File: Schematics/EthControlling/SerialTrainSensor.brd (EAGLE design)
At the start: 13 x 23 mm, 17 parts, among them IC2 LMV358

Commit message: identify schematics by the order number on schematics and submitted gerber files
Signed-off-by: sosoru <siva6991@yahoo.co.jp>
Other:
- board text added: "D53371"
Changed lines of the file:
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@@
 <text x="11.5824" y="7.7216" size="0.6096" layer="21" font="vector" rot="R270">TrSensor Rev.B</text>
 <text x="10.3632" y="2.8448" size="0.6096" layer="21" font="vector" rot="R270">T.U.S.</text>
+<text x="8.7376" y="11.5824" size="1.016" layer="26" rot="MR0">D53371</text>
 </plain>
 <attributes>

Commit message: debuging device transfer
Signed-off-by: sosoru <siva6991@yahoo.co.jp>
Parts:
- R1, R5: value (none) -> 1k
- R2, R6: value (none) -> 100k
- R3, R4: value (none) -> 33k
- R7: value (none) -> 10k
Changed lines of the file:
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@@
 <attribute name="VALUE" x="3.6282" y="0.256" size="0.6096" layer="21" font="vector" rot="R90"/>
 </element>
-<element name="R3" library="rcl" package="R0603" value="" x="4.3688" y="16.8656" smashed="yes" rot="R180">
+<element name="R3" library="rcl" package="R0603" value="33k" x="4.3688" y="16.8656" smashed="yes" rot="R180">
 <attribute name="NAME" x="2.9718" y="17.2466" size="0.6096" layer="25" font="vector" rot="R180"/>
 <attribute name="VALUE" x="5.0038" y="18.7706" size="1.27" layer="27" rot="R180"/>
 </element>
-<element name="R1" library="rcl" package="R0603" value="" x="4.3688" y="18.1864" smashed="yes" rot="R180">
+<element name="R1" library="rcl" package="R0603" value="1k" x="4.3688" y="18.1864" smashed="yes" rot="R180">
 <attribute name="NAME" x="2.9718" y="18.5674" size="0.6096" layer="25" font="vector" rot="R180"/>
 <attribute name="VALUE" x="5.0038" y="20.0914" size="1.27" layer="27" rot="R180"/>
 </element>
-<element name="R2" library="rcl" package="R0603" value="" x="2.032" y="20.7264" smashed="yes" rot="R90">
+<element name="R2" library="rcl" package="R0603" value="100k" x="2.032" y="20.7264" smashed="yes" rot="R90">
 <attribute name="NAME" x="1.397" y="20.0914" size="0.6096" layer="25" font="vector" rot="R90"/>
 <attribute name="VALUE" x="3.937" y="20.0914" size="1.27" layer="27" rot="R90"/>
 </element>
-<element name="R6" library="rcl" package="R0603" value="" x="6.9088" y="2.032" smashed="yes" rot="R270">
+<element name="R6" library="rcl" package="R0603" value="100k" x="6.9088" y="2.032" smashed="yes" rot="R270">
 <attribute name="NAME" x="7.5438" y="2.667" size="0.6096" layer="25" font="vector" rot="R270"/>
 <attribute name="VALUE" x="5.0038" y="2.667" size="1.27" layer="27" rot="R270"/>
 </element>
-<element name="R4" library="rcl" package="R0603" value="" x="4.064" y="6.9088" smashed="yes" rot="R180">
+<element name="R4" library="rcl" package="R0603" value="33k" x="4.064" y="6.9088" smashed="yes" rot="R180">
 <attribute name="NAME" x="2.667" y="7.493" size="0.6096" layer="25" font="vector" rot="R180"/>
 <attribute name="VALUE" x="4.699" y="8.8138" size="1.27" layer="27" rot="R180"/>
 </element>
-<element name="R5" library="rcl" package="R0603" value="" x="4.064" y="5.4864" smashed="yes">
+<element name="R5" library="rcl" package="R0603" value="1k" x="4.064" y="5.4864" smashed="yes">
 <attribute name="NAME" x="1.6002" y="5.5118" size="0.6096" layer="25" font="vector"/>
 <attribute name="VALUE" x="3.429" y="3.5814" size="1.27" layer="27"/>
@@
 <element name="SMD1" library="myparts" package="SERIAL_5_HALF" value="SERIAL_SENSORHALF" x="11.7856" y="11.7856" rot="R90"/>
 <element name="SMD2" library="myparts" package="SERIAL_5_HALF" value="SERIAL_SENSORHALF" x="1.2192" y="11.7856" rot="R90"/>
-<element name="R7" library="rcl" package="R0603" value="" x="8.636" y="12.5984" smashed="yes" rot="R180">
+<element name="R7" library="rcl" package="R0603" value="10k" x="8.636" y="12.5984" smashed="yes" rot="R180">
 <attribute name="NAME" x="10.0838" y="13.9954" size="0.6096" layer="25" font="vector" rot="R180"/>
 <attribute name="VALUE" x="9.271" y="14.5034" size="1.27" layer="27" rot="R180"/>

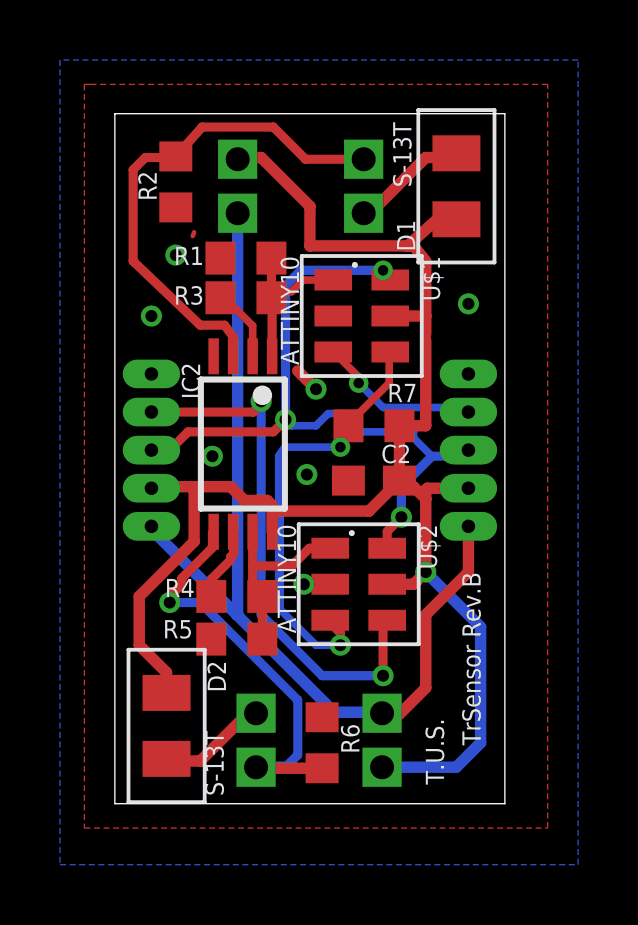
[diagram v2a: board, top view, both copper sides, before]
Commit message: fixed train sensor board
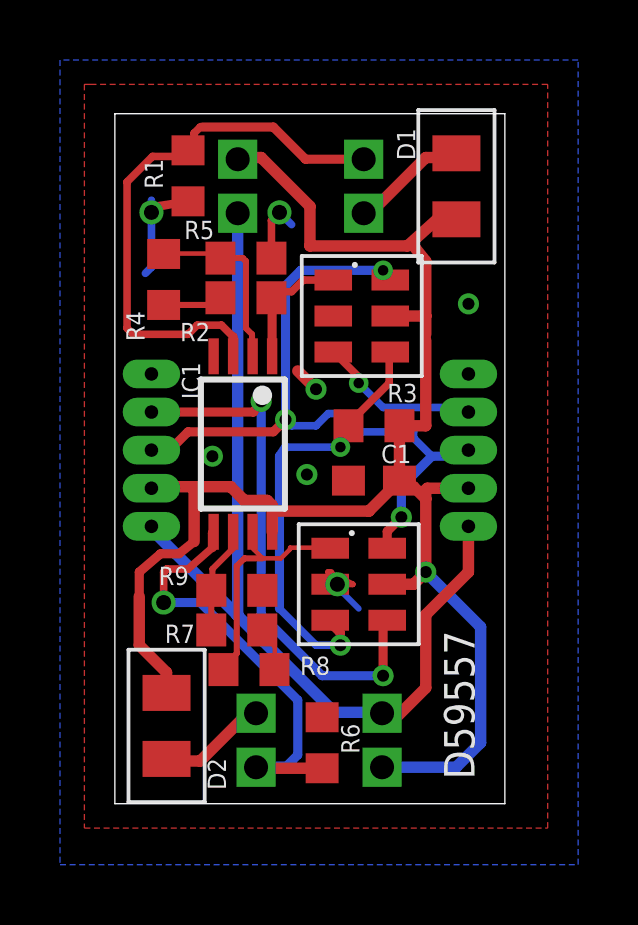
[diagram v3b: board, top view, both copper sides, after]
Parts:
- removed U$101: TPR-105F, myparts:TPR-105F
- added R8: 33k, rcl:R0603
- added R9: 1k, rcl:R0603
- added U$3: ATTINY10, myparts:SOT-23
- R1: value 1k -> 10k
- R2: value 100k -> 33k
- R3: value 33k -> 10k
- R6: value 100k -> 10k
- R7: value 10k -> 33k
- U$1: value ATTINY10 -> TPR-105F; device myparts:SOT-23 -> myparts:TPR-105F
- moved R5 12.7 mm to (4.37, 18.2)
- moved R4 10.8 mm to (1.63, 17.5), turned to 90 degrees
- moved U$2 8.94 mm to (8.23, 16.3)
- moved R7 8.20 mm to (4.06, 5.79)
- moved R3 6.03 mm to (8.64, 12.6)
- moved U$1 5.59 mm to (5.59, 21.2), flipped to the bottom, turned to 180 degrees
- moved R2 4.51 mm to (4.37, 16.9), turned to 180 degrees
- moved R1 3.35 mm to (2.44, 20.9), turned to 90 degrees
- renumbered C2 to C1, IC2 to IC1, U$100 to U$4
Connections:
- new net N$8: R2.2, R4.1
- new net N$9: R7.1, R8.2
- net CHAIN_IN: now also U$2.3; no longer U$1.3
- net CHAIN_OUT: now also U$3.4; no longer U$2.4
- net GND: now also R1.1, R5.2, R9.1, U$3.2; no longer R1.2, R2.1, R5.1, U$1.2
- net N$1: now also U$1.1; no longer U$101.1
- net N$2: now also R1.2, U$1.4; no longer R2.2, U$101.4
- net N$4: now also R3.2, U$2.4, U$3.3; no longer R7.2, U$1.4, U$2.3
- net N$6: now also R4.2, R5.1; no longer R3.2
- net N$7: now also R7.2, R9.2; no longer R4.2
- net SENS_A: now also R2.1, U$2.1; no longer R1.1, R3.1, U$1.1
- net SENS_B: now also R8.1, U$3.1; no longer R4.1, R5.2, U$2.1
- net TRANS: now also U$3.6; no longer U$1.6
- net VCC: now also R3.1, U$1.3, U$3.5; no longer R7.1, U$1.5, U$101.3
- net VLED: now also U$1.2; no longer U$101.2
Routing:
- net GND: track 1.04 -> 11.3 mm
- net N$6: track 2.48 -> 6.22 mm
- net N$2: track 16.8 -> 19.1 mm
- net N$7: track 2.47 -> 4.51 mm
- net N$8: track 0.00 -> 1.99 mm
- net N$9: track 0.00 -> 1.75 mm
- net SENS_B: track 6.54 -> 8.03 mm
- net SENS_A: track 6.17 -> 4.75 mm
- net N$5: track 14.2 -> 14.9 mm
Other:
- board text added: "D59557"
- board text added: "TrSensor Rev.C"
- board text removed: "D53371"
- board text removed: "T.U.S."
- board text removed: "TrSensor Rev.B"

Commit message: ditto
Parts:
- R1, R6: value 10k -> 1k
- R2, R8: value 33k -> 3.3k
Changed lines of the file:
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@@
 <attribute name="NAME" x="3.7044" y="0.4592" size="0.6096" layer="21" font="vector" rot="R90"/>
 </element>
-<element name="R2" library="rcl" package="R0603" value="33k" x="4.3688" y="16.8656" smashed="yes" rot="R180">
+<element name="R2" library="rcl" package="R0603" value="3.3k" x="4.3688" y="16.8656" smashed="yes" rot="R180">
 <attribute name="NAME" x="3.175" y="16.0274" size="0.6096" layer="25" font="vector" rot="R180"/>
 <attribute name="VALUE" x="5.0038" y="18.7706" size="1.27" layer="27" rot="R180"/>
@@
 <attribute name="VALUE" x="3.7338" y="16.2814" size="1.27" layer="27"/>
 </element>
-<element name="R1" library="rcl" package="R0603" value="10k" x="2.4384" y="20.9296" smashed="yes" rot="R90">
+<element name="R1" library="rcl" package="R0603" value="1k" x="2.4384" y="20.9296" smashed="yes" rot="R90">
 <attribute name="NAME" x="1.6002" y="20.4978" size="0.6096" layer="25" font="vector" rot="R90"/>
 <attribute name="VALUE" x="4.3434" y="20.2946" size="1.27" layer="27" rot="R90"/>
 </element>
-<element name="R6" library="rcl" package="R0603" value="10k" x="6.9088" y="2.032" smashed="yes" rot="R270">
+<element name="R6" library="rcl" package="R0603" value="1k" x="6.9088" y="2.032" smashed="yes" rot="R270">
 <attribute name="NAME" x="7.5438" y="2.667" size="0.6096" layer="25" font="vector" rot="R270"/>
 <attribute name="VALUE" x="5.0038" y="2.667" size="1.27" layer="27" rot="R270"/>
@@
 <attribute name="VALUE" x="3.5306" y="16.8402" size="1.27" layer="27" rot="R90"/>
 </element>
-<element name="R8" library="rcl" package="R0603" value="33k" x="4.4704" y="4.4704" smashed="yes">
+<element name="R8" library="rcl" package="R0603" value="3.3k" x="4.4704" y="4.4704" smashed="yes">
 <attribute name="NAME" x="6.1722" y="4.2926" size="0.6096" layer="25" font="vector"/>
 <attribute name="VALUE" x="3.8354" y="2.5654" size="1.27" layer="27"/>

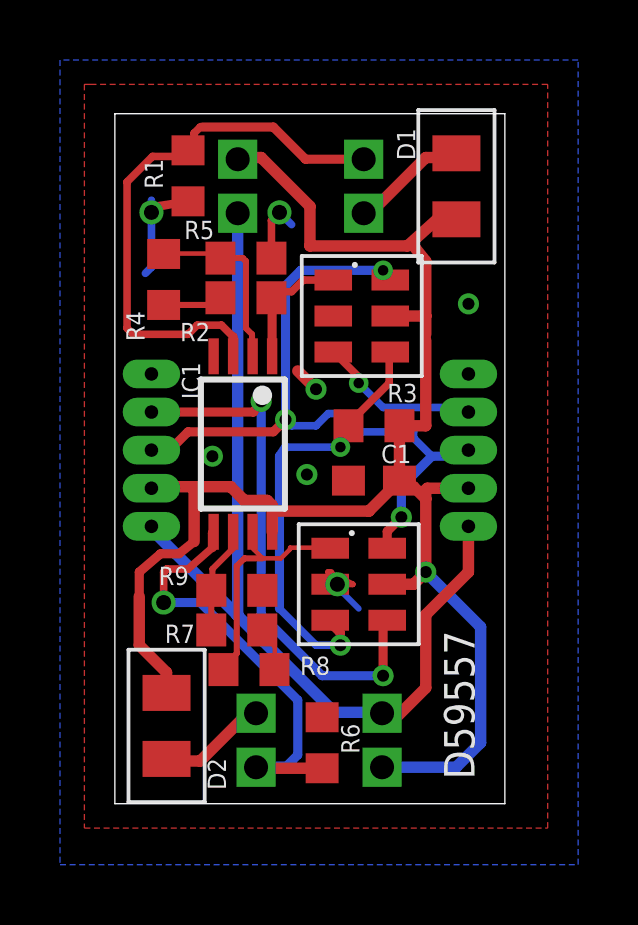
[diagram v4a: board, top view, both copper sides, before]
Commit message: add a resistor to transfer on TrSensor
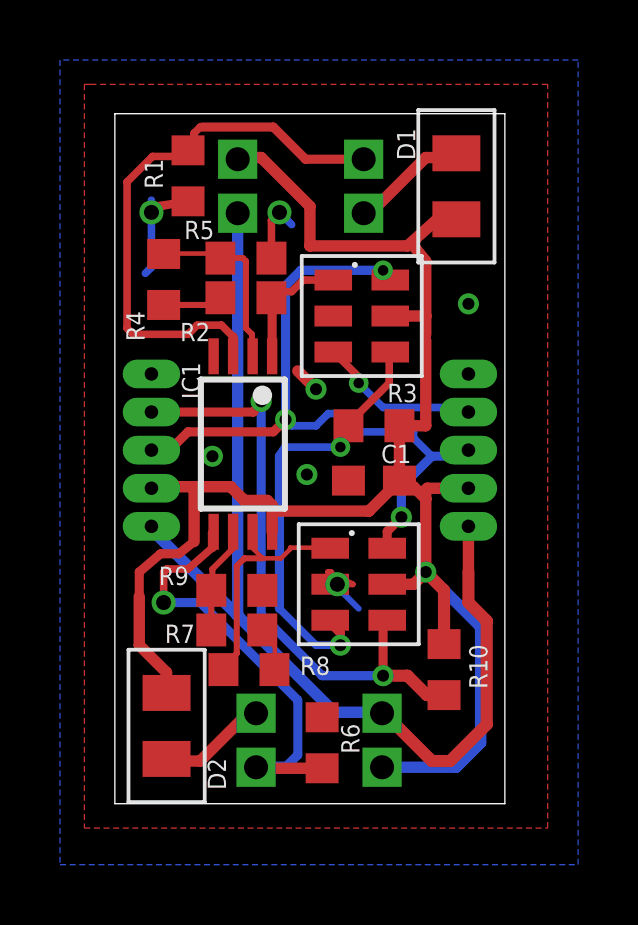
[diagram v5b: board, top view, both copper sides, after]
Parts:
- added R10: 10k, rcl:R0603
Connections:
- net CHAIN_OUT: now also R10.2
- net VCC: now also R10.1
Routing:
- net VLED: track 31.7 -> 36.3 mm
- net VCC: track 55.3 -> 57.9 mm
- net CHAIN_OUT: track 17.8 -> 20.1 mm
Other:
- board text added: "D61606"
- board text added: "TrSensor Rev.C-2'"
- board text removed: "D59557"
- board text removed: "TrSensor Rev.C"
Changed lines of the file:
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@@
 <wire x1="13" y1="23" x2="0" y2="23" width="0" layer="20"/>
 <wire x1="0" y1="23" x2="0" y2="0" width="0" layer="20"/>
-<text x="2.6416" y="22.352" size="0.6096" layer="22" font="vector" rot="MR270">TrSensor Rev.C</text>
+<text x="2.8448" y="22.352" size="0.6096" layer="22" font="vector" rot="MR270">TrSensor Rev.C-2'</text>
 <rectangle x1="2.82575" y1="6.31825" x2="2.86385" y2="6.35635" layer="26" rot="R90"/>
 <rectangle x1="2.9972" y1="6.2992" x2="3.0734" y2="6.3373" layer="26" rot="R90"/>
@@
 <rectangle x1="12.3317" y1="8.0137" x2="12.4079" y2="8.0518" layer="26" rot="R90"/>
 <rectangle x1="12.54125" y1="8.03275" x2="12.57935" y2="8.07085" layer="26" rot="R90"/>
-<text x="11.9888" y="0.8128" size="1.016" layer="25" rot="R90">D59557</text>
+<text x="12.3952" y="0.4064" size="0.4064" layer="22" rot="MR0">D61606</text>
 </plain>
 <attributes>
@@
 <attribute name="VALUE" x="3.8354" y="2.5654" size="1.27" layer="27"/>
 </element>
+<element name="R10" library="rcl" package="R0603" value="10k" x="10.9728" y="4.4704" smashed="yes" rot="R270">
+<attribute name="NAME" x="11.811" y="5.3086" size="0.6096" layer="25" font="vector" rot="R270"/>
+<attribute name="VALUE" x="9.0678" y="5.1054" size="1.27" layer="27" rot="R270"/>
+</element>
 </elements>
 <signals>
@@
 <wire x1="8.9408" y1="5.978" x2="9.078" y2="6.1152" width="0.3048" layer="1"/>
 <wire x1="4.8768" y1="6.2992" x2="4.8768" y2="13.4112" width="0.3048" layer="16"/>
+<contactref element="R10" pad="2"/>
+<wire x1="10.9728" y1="3.6204" x2="10.4004" y2="3.6204" width="0.4064" layer="1"/>
+<wire x1="10.4004" y1="3.6204" x2="9.7536" y2="4.2672" width="0.4064" layer="1"/>
+<wire x1="9.7536" y1="4.2672" x2="8.9408" y2="4.2672" width="0.4064" layer="1"/>
 </signal>
 <signal name="GND">
@@
 <wire x1="1.524" y1="8.3312" x2="0.8128" y2="7.7216" width="0.3048" layer="1"/>
 <wire x1="0.8128" y1="7.7216" x2="0.8128" y2="6.9088" width="0.3048" layer="1"/>
+<contactref element="R10" pad="1"/>
+<wire x1="10.9728" y1="5.3204" x2="10.9728" y2="7.112" width="0.4064" layer="1"/>
+<wire x1="10.9728" y1="7.112" x2="10.3632" y2="7.7216" width="0.4064" layer="1"/>
 </signal>
 <signal name="VLED" class="1">
@@
 <contactref element="SMD1" pad="P$1"/>
 <contactref element="SMD2" pad="P$1"/>
-<wire x1="11.7856" y1="7.7216" x2="10.3632" y2="6.2992" width="0.381" layer="1"/>
-<wire x1="10.3632" y1="6.2992" x2="10.3632" y2="3.8608" width="0.381" layer="1"/>
-<wire x1="10.3632" y1="3.8608" x2="9.3472" y2="2.8448" width="0.381" layer="1"/>
 <wire x1="9.3472" y1="2.8448" x2="9.0772" y2="2.8448" width="0.381" layer="1"/>
 <wire x1="9.0772" y1="2.8448" x2="8.9064" y2="3.0156" width="0.381" layer="1"/>
@@
 <wire x1="4.0936" y1="6.3288" x2="4.064" y2="6.2992" width="0.381" layer="16"/>
 <wire x1="1.2192" y1="9.2456" x2="1.2192" y2="9.144" width="0.381" layer="16"/>
+<wire x1="11.7856" y1="7.7216" x2="11.7856" y2="6.7056" width="0.4064" layer="1"/>
+<wire x1="11.7856" y1="6.7056" x2="12.3952" y2="6.096" width="0.4064" layer="1"/>
+<wire x1="12.3952" y1="6.096" x2="12.3952" y2="2.6416" width="0.4064" layer="1"/>
+<wire x1="12.3952" y1="2.6416" x2="11.176" y2="1.4224" width="0.4064" layer="1"/>
+<wire x1="11.176" y1="1.4224" x2="10.5664" y2="1.4224" width="0.4064" layer="1"/>
+<wire x1="10.5664" y1="1.4224" x2="9.2964" y2="2.6924" width="0.4064" layer="1"/>
+<wire x1="9.2964" y1="2.6924" x2="8.9408" y2="3.048" width="0.4064" layer="1"/>
+<wire x1="9.2964" y1="2.6924" x2="8.9064" y2="3.0156" width="0.381" layer="1"/>
 </signal>
 <signal name="N$4">
